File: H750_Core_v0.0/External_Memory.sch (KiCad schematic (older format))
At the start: 12 parts, among them U13 TC58BVG1S3HTA00, U14 IS25LP256D

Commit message: PCB layout finished
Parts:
- JP22, JP23: footprint Resistor_SMD:R_0603_1608Metric -> H750_Core:JP
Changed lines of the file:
@@
 F 0 "JP22" H 4400 5185 50  0000 C CNN
 F 1 "Jumper_2_Open" H 4400 5094 50  0000 C CNN
-F 2 "Resistor_SMD:R_0603_1608Metric" H 4400 4950 50  0001 C CNN
+F 2 "H750_Core:JP" H 4400 4950 50  0001 C CNN
 F 3 "~" H 4400 4950 50  0001 C CNN
 	1    4400 4950
@@
 F 0 "JP23" H 4650 4745 50  0000 C CNN
 F 1 "Jumper_2_Bridged" H 4650 4654 50  0000 C CNN
-F 2 "Resistor_SMD:R_0603_1608Metric" H 4650 4550 50  0001 C CNN
+F 2 "H750_Core:JP" H 4650 4550 50  0001 C CNN
 F 3 "~" H 4650 4550 50  0001 C CNN
 	1    4650 4550

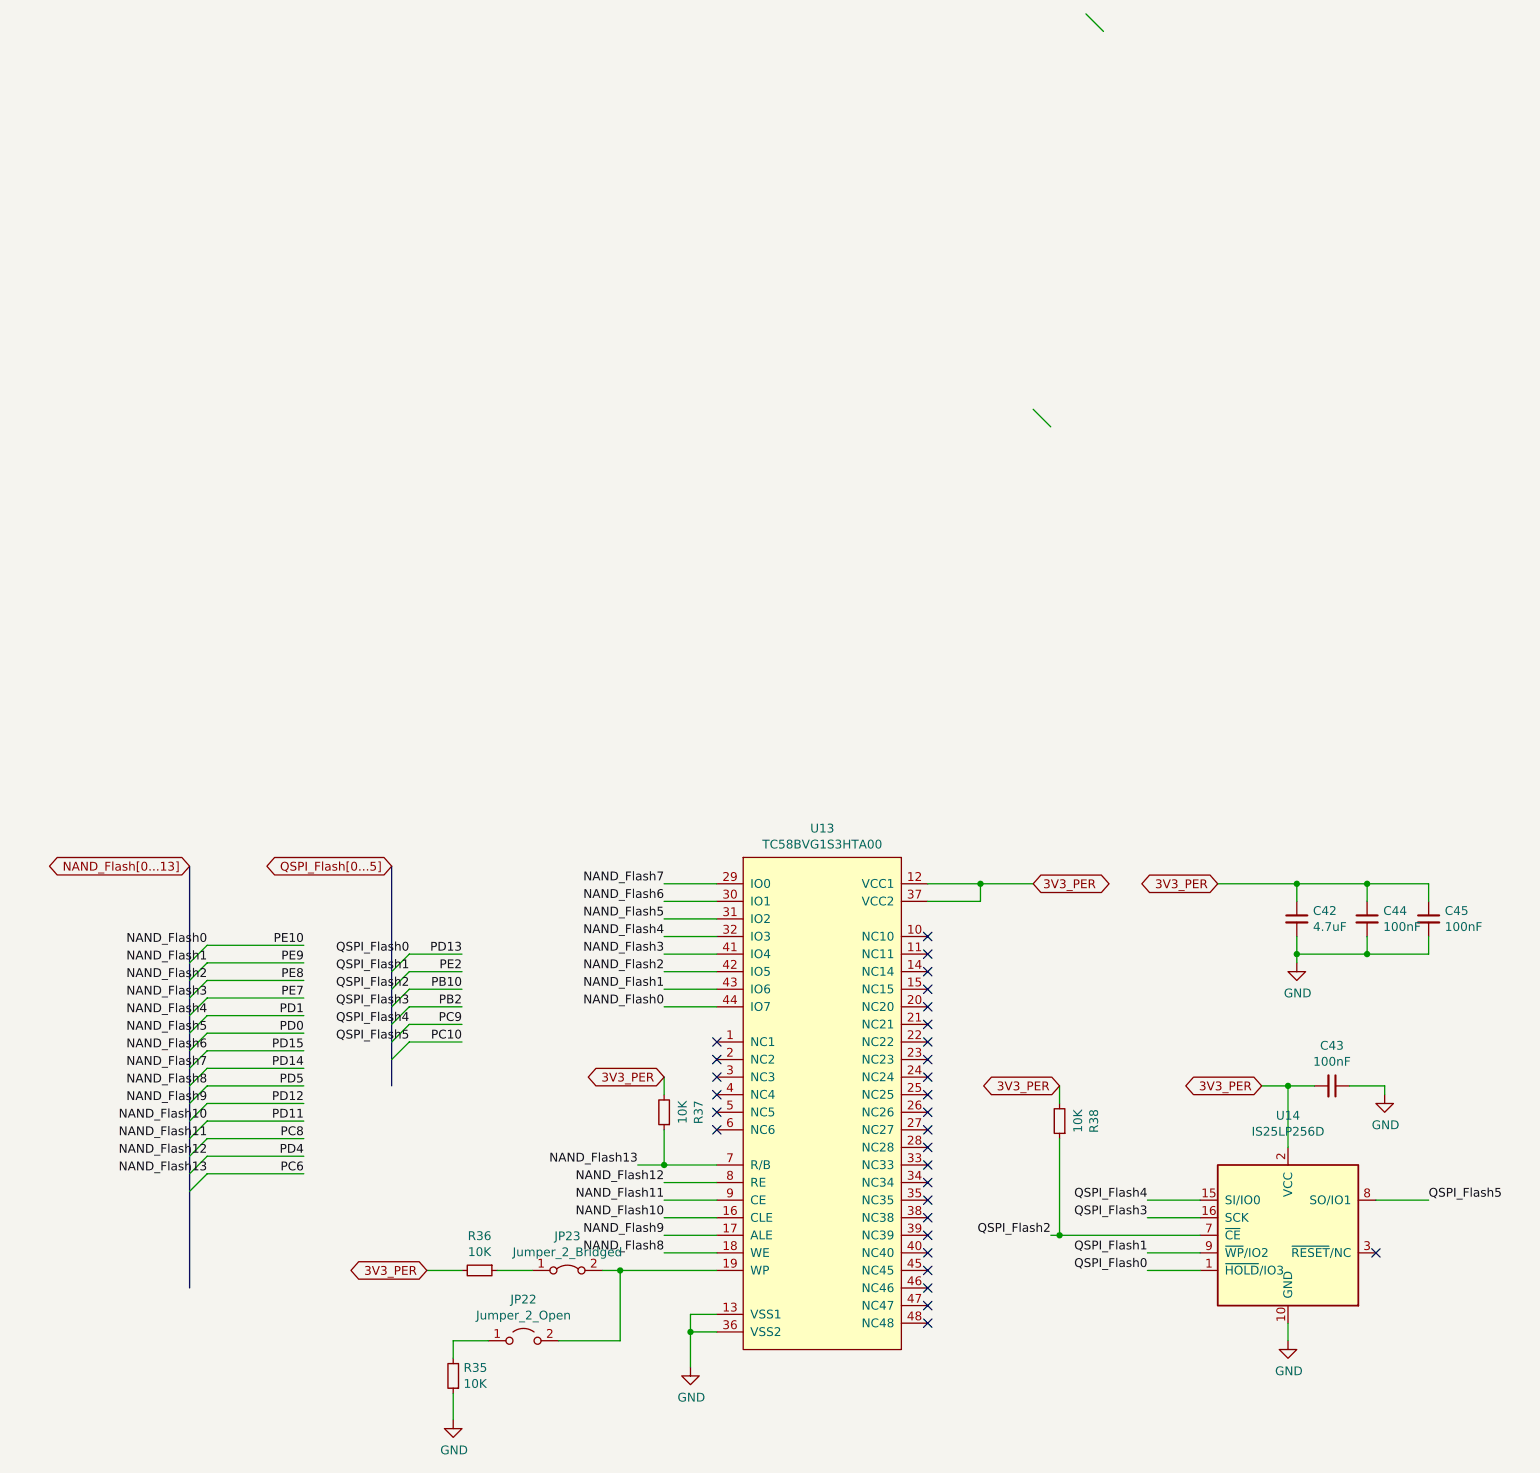
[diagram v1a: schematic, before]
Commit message: 修改编程接口
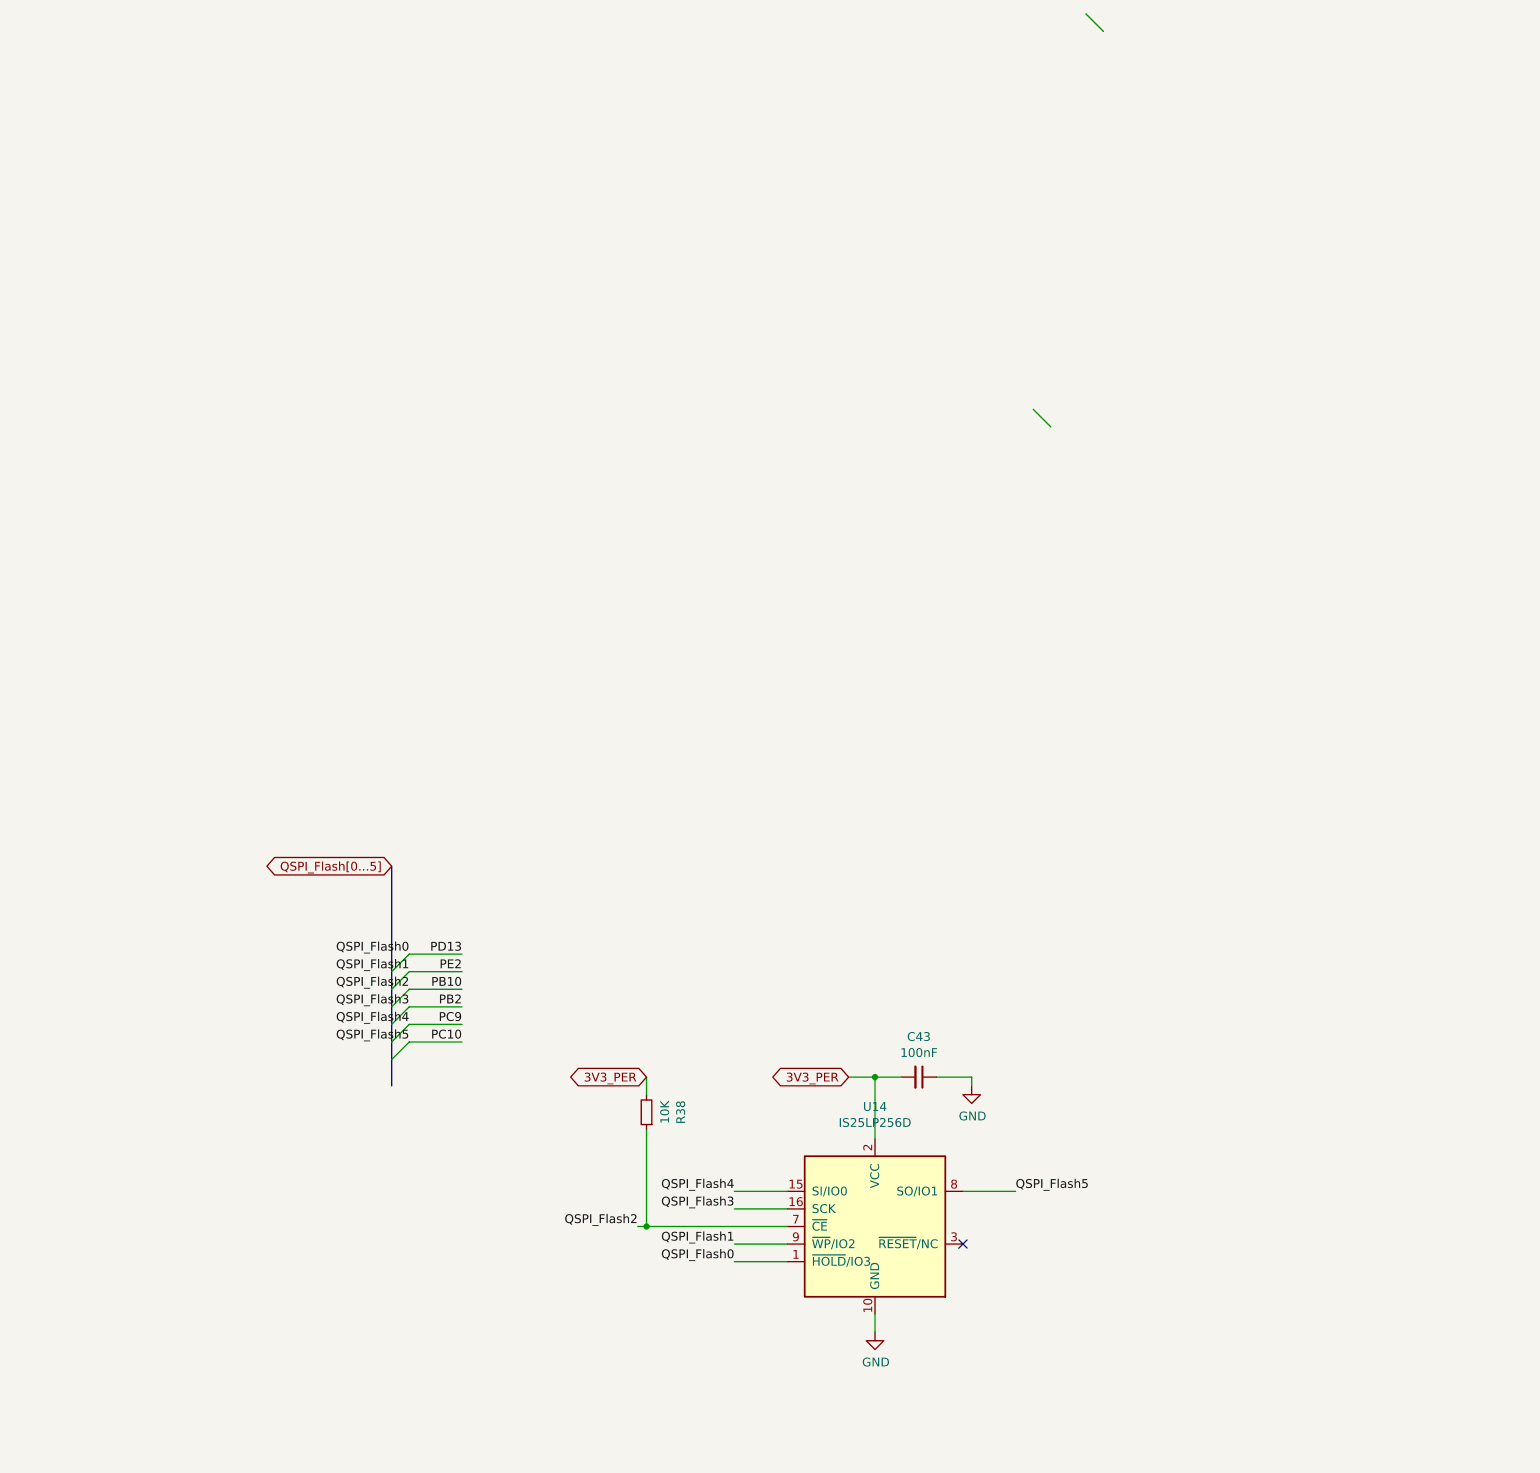
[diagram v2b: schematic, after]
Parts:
- removed C42: 4.7uF, Capacitor_SMD:C_0603_1608Metric, symbol Device:C_Small
- removed C44, C45: 100nF, Capacitor_SMD:C_0603_1608Metric, symbol Device:C_Small
- removed JP22: Jumper_2_Open, H750_Core:JP, symbol Jumper:Jumper_2_Open
- removed JP23: Jumper_2_Bridged, H750_Core:JP, symbol Jumper:Jumper_2_Bridged
- removed R35, R36, R37: 10K, Resistor_SMD:R_0603_1608Metric, symbol Device:R_Small
- removed U13: TC58BVG1S3HTA00, Package_SO:TSOP-I-48_18.4x12mm_P0.5mm, symbol CommonParts:TC58BVG1S3HTA00
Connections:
- no-connect marks 30 -> 1
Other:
- moved on the sheet: C43, R38, U14
